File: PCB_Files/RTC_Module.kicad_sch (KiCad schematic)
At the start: 20 parts, among them J1 DZ254W-11-06-65, U1 DS3231SN#T&R, U2 AMS1117-3.3, U3 PCF8563T, Y1 Q13FC13500004

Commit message: Continues with layout
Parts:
- added BT2: Battery_Cell, Battery:BatteryHolder_LINX_BAT-HLD-012-SMT, symbol Device:Battery_Cell
- added C6: 100nF/10V, Capacitor_SMD:C_0805_2012Metric, symbol Device:C
- added R7, R8: 4k7, Resistor_SMD:R_0603_1608Metric, symbol Device:R
- C4, C5: value 10uF/10V -> 12p5/10V
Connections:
- net 3.3V: now also U3.8 (VDD), BT2.1 (+), C6.1, R7.1, R8.1
- net GND: now also U3.4 (VSS), BT2.2 (-), C6.2
- net at U3.3 (~{INT}): now also R8.2
- net at U3.7 (CLKO): now also R7.2

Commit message: Finished PCB with new RTC.
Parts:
- removed BT1: Battery_Cell, Battery:BatteryHolder_LINX_BAT-HLD-012-SMT, symbol Device:Battery_Cell
- removed C1: 100n/10V, Capacitor_SMD:C_0603_1608Metric, symbol Device:C
- removed JP1: SolderJumper_2_Open, Jumper:SolderJumper-2_P1.3mm_Open_TrianglePad1.0x1.5mm, symbol Jumper:SolderJumper_2_Open
- removed R1, R2, R3, R4: 4k7, Resistor_SMD:R_0603_1608Metric, symbol Device:R
- removed U1: DS3231SN#T&R, Package_SO:SOIC-16W_7.5x10.3mm_P1.27mm, symbol Timer_RTC:DS3231M
- C3: renamed from C6; footprint Capacitor_SMD:C_0805_2012Metric -> Capacitor_SMD:C_0603_1608Metric
- C4: renamed from C5; footprint Capacitor_SMD:C_0805_2012Metric -> Capacitor_SMD:C_0603_1608Metric
- C5: renamed from C4; footprint Capacitor_SMD:C_0805_2012Metric -> Capacitor_SMD:C_0603_1608Metric
- renumbered BT2 to BT1, C2 to C1, C3 to C2, R6 to R1, R5 to R2, R7 to R3, R8 to R4, U2 to U1, U3 to U2
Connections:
- net 32KHZ is gone; now on net CLK: J1.5 (Pin_5)
- net SQW is gone; now on net INT: J1.6 (Pin_6)
- net OSCI: now reaches C4.1, U2.1 (OSCI), Y1.1
- net OSCO: now reaches C5.1, U2.2 (OSCO), Y1.2
- net INT: now reaches R4.2, U2.3 (~{INT})
- net CLK: now reaches R3.2, U2.7 (CLKO)
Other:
- moved on the sheet: R3, R4

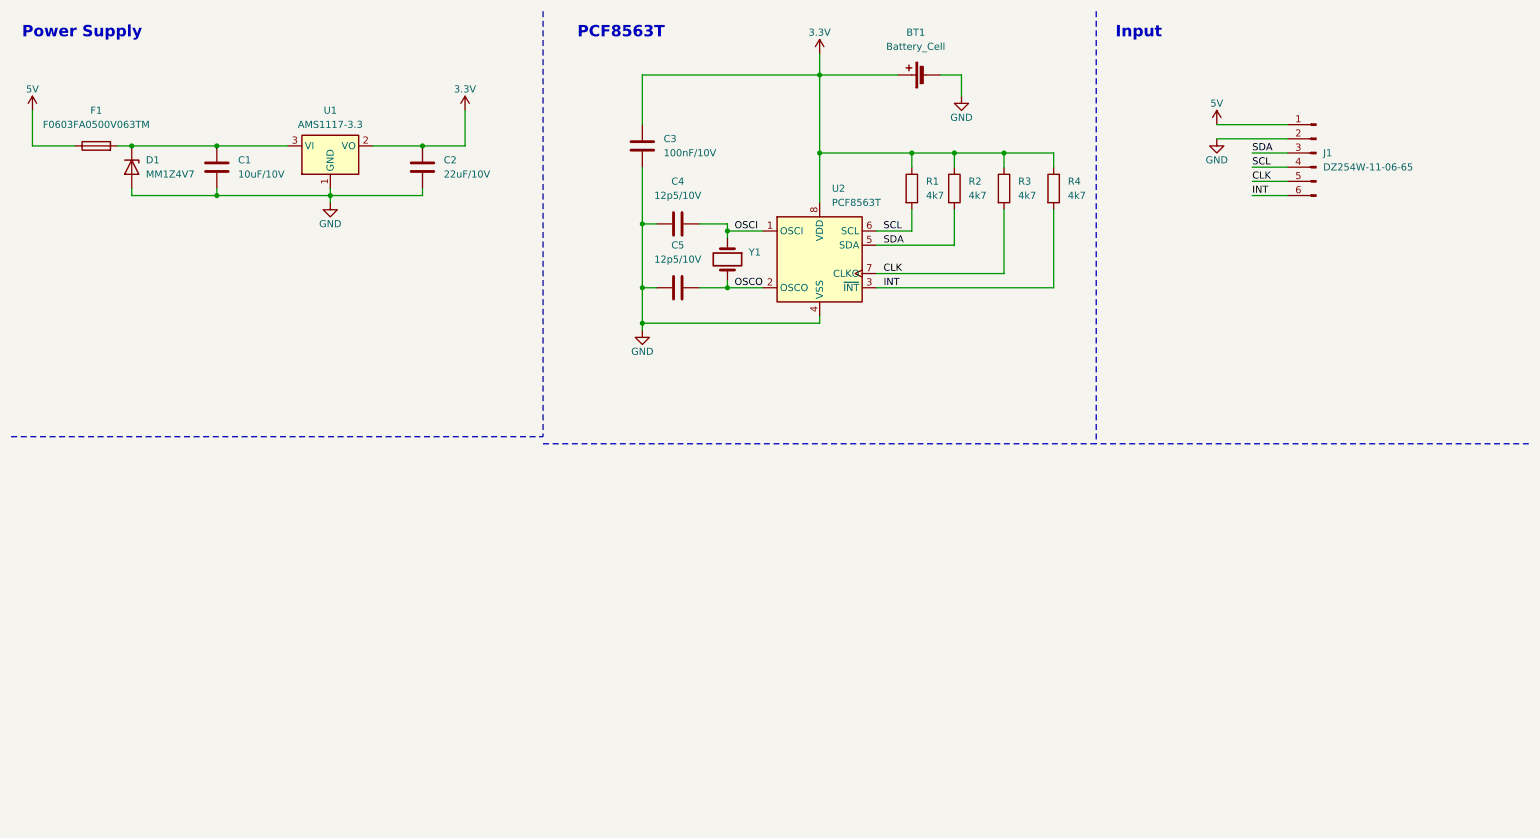
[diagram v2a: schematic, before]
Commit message: Added step of DCDC. Updated gitignore. Now version with battery cell on top side.
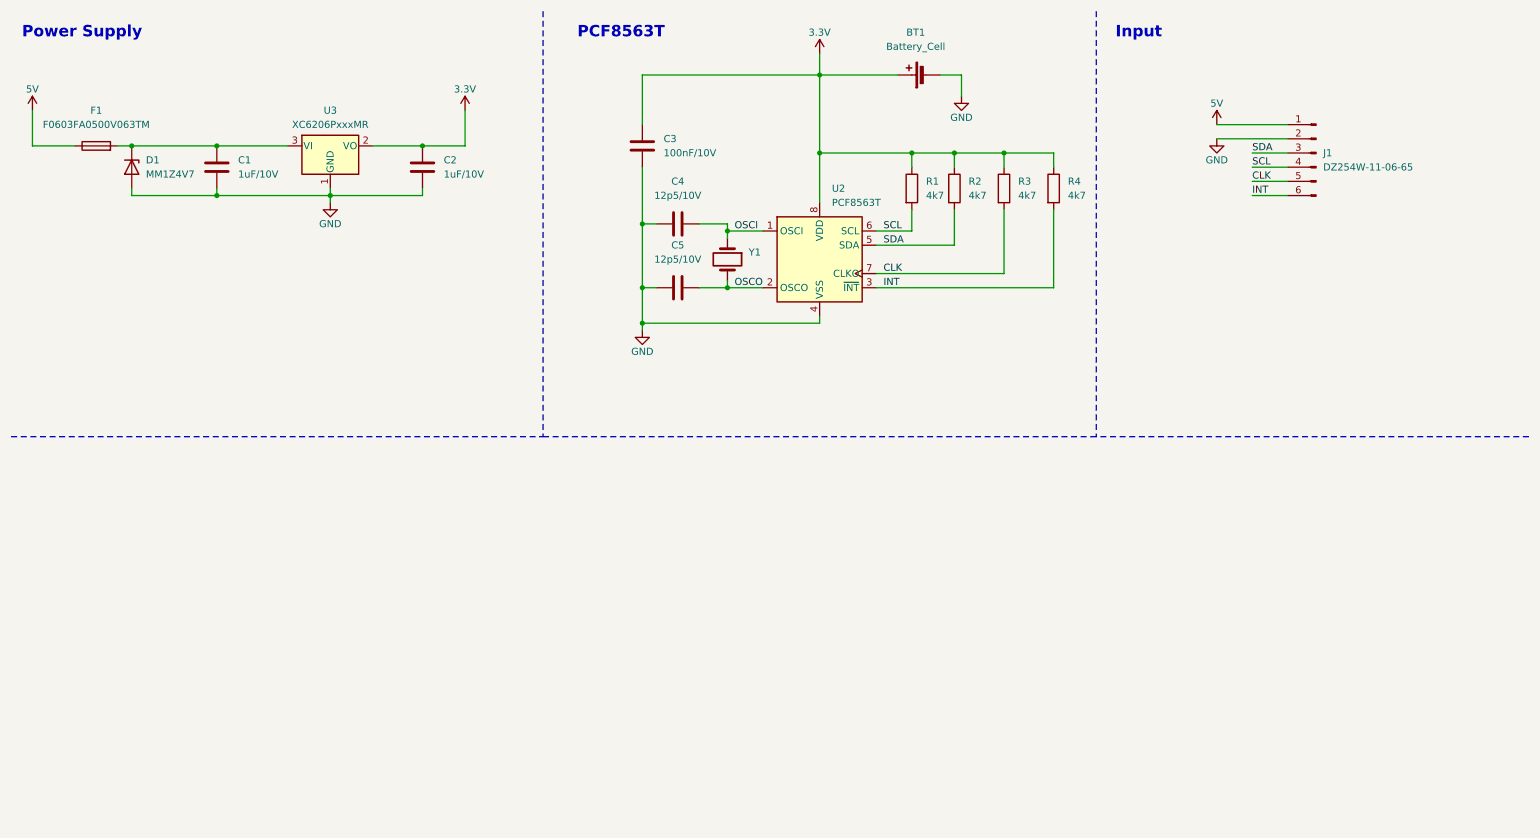
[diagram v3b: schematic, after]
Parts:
- removed U1: AMS1117-3.3, Package_TO_SOT_SMD:SOT-223-3_TabPin2, symbol Regulator_Linear:AMS1117-3.3
- added U3: XC6206PxxxMR, Package_TO_SOT_SMD:SOT-23-3, symbol Regulator_Linear:XC6206PxxxMR
- C1: value 10uF/10V -> 1uF/10V
- C2: value 22uF/10V -> 1uF/10V
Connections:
- net 3.3V: now also U3.2 (VO)
- net GND: now also U3.1 (GND)
- net at C1.1, D1.1 (K), F1.2: now also U3.3 (VI)
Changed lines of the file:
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@@
 	(polyline
 		(pts
-			(xy 107.95 90.17) (xy 207.01 90.17)
+			(xy 107.95 88.9) (xy 207.01 88.9)
 		)
 		(stroke
@@
 	(polyline
 		(pts
-			(xy 207.01 12.7) (xy 207.01 90.17)
+			(xy 207.01 12.7) (xy 207.01 88.9)
 		)
 		(stroke
@@
 	(polyline
 		(pts
-			(xy 284.48 90.17) (xy 207.01 90.17)
+			(xy 284.48 88.9) (xy 207.01 88.9)
 		)
 		(stroke
@@
 			)
 		)
-		(property "Value" "10uF/10V"
+		(property "Value" "1uF/10V"
 			(at 53.34 41.9099 0)
 			(effects
@@
 	)
 	(symbol
+		(lib_id "Regulator_Linear:XC6206PxxxMR")
+		(at 69.85 36.83 0)
+		(unit 1)
+		(exclude_from_sim no)
+		(in_bom yes)
+		(on_board yes)
+		(dnp no)
+		(fields_autoplaced yes)
+		(property "Reference" "U3"
+			(at 69.85 30.48 0)
+			(effects
+				(font
+					(size 1.27 1.27)
+				)
+			)
+		)
+		(property "Value" "XC6206PxxxMR"
+			(at 69.85 33.02 0)
+			(effects
+				(font
+					(size 1.27 1.27)
+				)
+			)
+		)
+		(property "Footprint" "Package_TO_SOT_SMD:SOT-23-3"
+			(at 69.85 31.115 0)
+			(effects
+				(font
+					(size 1.27 1.27)
+					(italic yes)
+				)
+				(hide yes)
+			)
+		)
+		(property "Datasheet" "https://www.torexsemi.com/file/xc6206/XC6206.pdf"
+			(at 69.85 36.83 0)
+			(effects
+				(font
+					(size 1.27 1.27)
+				)
+				(hide yes)
+			)
+		)
+		(property "Description" "Positive 60-250mA Low Dropout Regulator, Fixed Output, SOT-23"
+			(at 69.85 36.83 0)
+			(effects
+				(font
+					(size 1.27 1.27)
+				)
+				(hide yes)
+			)
+		)
+		(pin "3"
+		)
+		(pin "1"
+		)
+		(pin "2"
+		)
+		(instances
+			(project "RTC_Module"
+				(path "/3db6da75-e5f1-4a4e-a849-4536ae13a301"
+					(reference "U3")
+					(unit 1)
+				)
+			)
+		)
+	)
+	(symbol
 		(lib_id "Device:C")
 		(at 132.08 50.8 270)
@@
 			)
 		)
-		(property "Description" "Unpolarized capacitor"
+		(property "Description" "CL10C120JB8NNNC"
 			(at 132.08 50.8 0)
 			(effects
@@
 			)
 		)
-		(property "Description" "Unpolarized capacitor"
+		(property "Description" "CL10C120JB8NNNC"
 			(at 132.08 62.23 0)
 			(effects
@@
 	)
 	(symbol
-		(lib_id "Regulator_Linear:AMS1117-3.3")
-		(at 69.85 36.83 0)
-		(unit 1)
-		(exclude_from_sim no)
-		(in_bom yes)
-		(on_board yes)
-		(dnp no)
-		(property "Reference" "U1"
-			(at 69.85 30.48 0)
-			(effects
-				(font
-					(size 1.27 1.27)
-				)
-			)
-		)
-		(property "Value" "AMS1117-3.3"
-			(at 69.85 33.02 0)
-			(effects
-				(font
-					(size 1.27 1.27)
-				)
-			)
-		)
-		(property "Footprint" "Package_TO_SOT_SMD:SOT-223-3_TabPin2"
-			(at 69.85 31.75 0)
-			(effects
-				(font
-					(size 1.27 1.27)
-				)
-				(hide yes)
-			)
-		)
-		(property "Datasheet" "http://www.advanced-monolithic.com/pdf/ds1117.pdf"
-			(at 72.39 43.18 0)
-			(effects
-				(font
-					(size 1.27 1.27)
-				)
-				(hide yes)
-			)
-		)
-		(property "Description" "1A Low Dropout regulator, positive, 3.3V fixed output, SOT-223"
-			(at 69.85 36.83 0)
-			(effects
-				(font
-					(size 1.27 1.27)
-				)
-				(hide yes)
-			)
-		)
-		(pin "2"
-		)
-		(pin "3"
-		)
-		(pin "1"
-		)
-		(instances
-			(project "RTC_Module"
-				(path "/3db6da75-e5f1-4a4e-a849-4536ae13a301"
-					(reference "U1")
-					(unit 1)
-				)
-			)
-		)
-	)
-	(symbol
 		(lib_id "power:+5V")
 		(at 228.6 33.02 0)
@@
 			)
 		)
-		(property "Value" "22uF/10V"
+		(property "Value" "1uF/10V"
 			(at 90.17 41.9099 0)
 			(effects

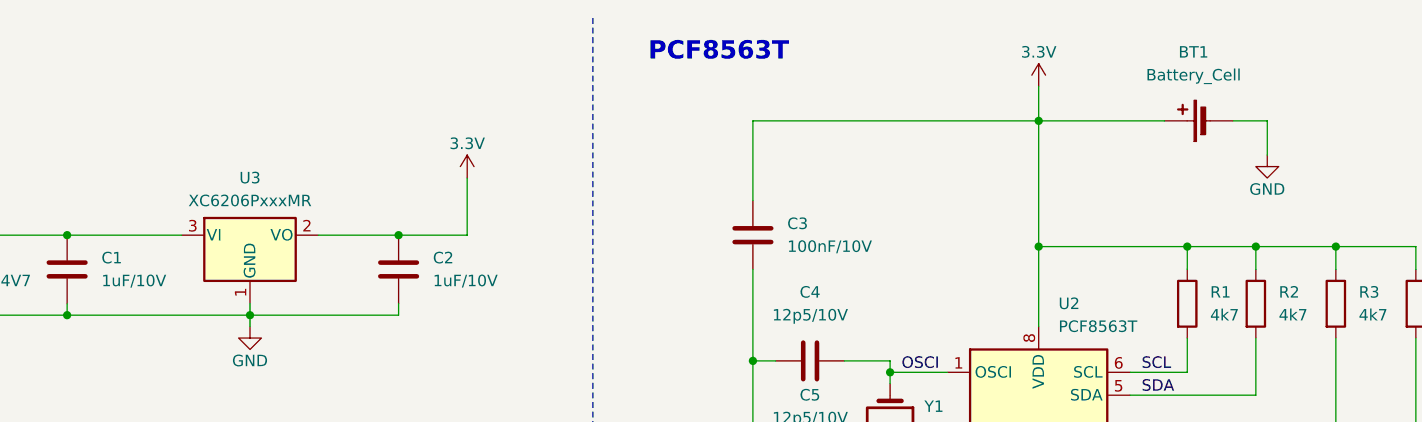
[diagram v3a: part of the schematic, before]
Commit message: Now finished and choose SMD battery.
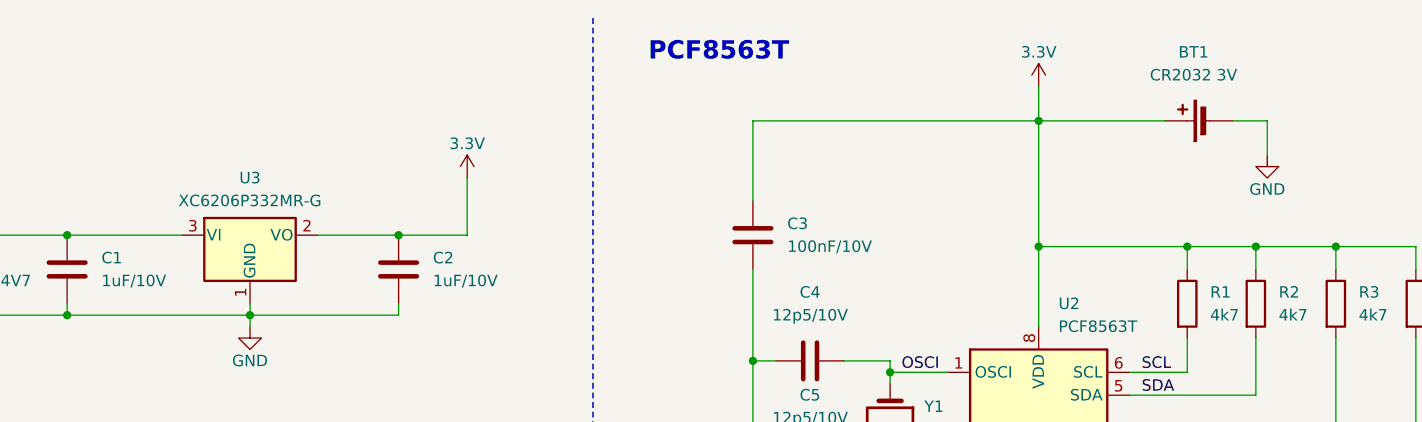
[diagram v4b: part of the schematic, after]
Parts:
- BT1: value Battery_Cell -> CR2032 3V
- U3: value XC6206PxxxMR -> XC6206P332MR-G
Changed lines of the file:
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@@
 			)
 		)
-		(property "Value" "XC6206PxxxMR"
+		(property "Value" "XC6206P332MR-G"
 			(at 69.85 33.02 0)
 			(effects
@@
 			)
 		)
-		(property "Value" "Battery_Cell"
+		(property "Value" "CR2032 3V"
 			(at 174.6885 19.05 90)
 			(effects

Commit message: This is ordered Version!!!!
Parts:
- BT1: value CR2032 3V -> MY-1220-03
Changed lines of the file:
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@@
 			)
 		)
-		(property "Value" "CR2032 3V"
+		(property "Value" "MY-1220-03"
 			(at 174.6885 19.05 90)
 			(effects
